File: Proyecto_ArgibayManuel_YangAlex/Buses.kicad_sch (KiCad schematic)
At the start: 6 parts, among them U6 MCP2551-I-P, X1 DB9, X2 DB9

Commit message: footprint
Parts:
- C5: renamed from C11; footprint (none) -> Capacitor_SMD:C_0805_2012Metric
- C6: renamed from C10; footprint (none) -> Capacitor_SMD:C_0805_2012Metric
- R10: renamed from R6; footprint (none) -> Resistor_THT:R_Axial_DIN0204_L3.6mm_D1.6mm_P1.90mm_Vertical
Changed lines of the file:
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@@
 		(dnp no)
 		(fields_autoplaced yes)
-		(property "Reference" "#PWR027"
+		(property "Reference" "#PWR020"
 			(at 55.88 53.34 0)
 			(effects
@@
 			(project "Proyecto_ArgibayManuel_YangAlex"
 				(path "/b2dde924-33f5-41ab-a1bf-811873450a89/310eabda-5b3c-4ba2-a48d-a60bed009d94"
-					(reference "#PWR027")
+					(reference "#PWR020")
 					(unit 1)
 				)
@@
 		(on_board yes)
 		(dnp no)
-		(property "Reference" "#PWR028"
+		(property "Reference" "#PWR019"
 			(at 35.56 74.93 0)
 			(effects
@@
 			(project "Proyecto_ArgibayManuel_YangAlex"
 				(path "/b2dde924-33f5-41ab-a1bf-811873450a89/310eabda-5b3c-4ba2-a48d-a60bed009d94"
-					(reference "#PWR028")
+					(reference "#PWR019")
 					(unit 1)
 				)
@@
 		(on_board yes)
 		(dnp no)
-		(property "Reference" "C10"
+		(property "Reference" "C6"
 			(at 145.288 58.166 90)
 			(effects
@@
 			)
 		)
-		(property "Footprint" ""
+		(property "Footprint" "Capacitor_SMD:C_0805_2012Metric"
 			(at 143.51 53.6448 0)
 			(effects
@@
 			(project "Proyecto_ArgibayManuel_YangAlex"
 				(path "/b2dde924-33f5-41ab-a1bf-811873450a89/310eabda-5b3c-4ba2-a48d-a60bed009d94"
-					(reference "C10")
+					(reference "C6")
 					(unit 1)
 				)
@@
 		(on_board yes)
 		(dnp no)
-		(property "Reference" "C11"
+		(property "Reference" "C5"
 			(at 144.78 38.608 90)
 			(effects
@@
 			)
 		)
-		(property "Footprint" ""
+		(property "Footprint" "Capacitor_SMD:C_0805_2012Metric"
 			(at 143.51 40.9448 0)
 			(effects
@@
 			(project "Proyecto_ArgibayManuel_YangAlex"
 				(path "/b2dde924-33f5-41ab-a1bf-811873450a89/310eabda-5b3c-4ba2-a48d-a60bed009d94"
-					(reference "C11")
+					(reference "C5")
 					(unit 1)
 				)
@@
 		(on_board yes)
 		(dnp no)
-		(property "Reference" "R6"
+		(property "Reference" "R10"
 			(at 137.16 46.9899 0)
 			(effects
@@
 			)
 		)
-		(property "Footprint" ""
+		(property "Footprint" "Resistor_THT:R_Axial_DIN0204_L3.6mm_D1.6mm_P1.90mm_Vertical"
 			(at 136.398 48.26 90)
 			(effects
@@
 			(project "Proyecto_ArgibayManuel_YangAlex"
 				(path "/b2dde924-33f5-41ab-a1bf-811873450a89/310eabda-5b3c-4ba2-a48d-a60bed009d94"
-					(reference "R6")
+					(reference "R10")
 					(unit 1)
 				)
@@
 		(on_board yes)
 		(dnp no)
-		(property "Reference" "#PWR07"
+		(property "Reference" "#PWR022"
 			(at 116.84 64.77 0)
 			(effects
@@
 			(project "Proyecto_ArgibayManuel_YangAlex"
 				(path "/b2dde924-33f5-41ab-a1bf-811873450a89/310eabda-5b3c-4ba2-a48d-a60bed009d94"
-					(reference "#PWR07")
+					(reference "#PWR022")
 					(unit 1)
 				)
@@
 		(on_board yes)
 		(dnp no)
-		(property "Reference" "#PWR022"
+		(property "Reference" "#PWR018"
 			(at 30.48 45.72 0)
 			(effects
@@
 			(project "Proyecto_ArgibayManuel_YangAlex"
 				(path "/b2dde924-33f5-41ab-a1bf-811873450a89/310eabda-5b3c-4ba2-a48d-a60bed009d94"
-					(reference "#PWR022")
-					(unit 1)
-				)
+					(reference "#PWR018")
+					(unit 1)
+				)

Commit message: sensor
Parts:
- removed X2: DB9, DB9:DB9, symbol DB9:DB9
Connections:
- net RC6 is gone; now on net GND: X1.3
- net CANH: now also X1.7
- net CANL: now also X1.2
- net GND: no longer X1.2
- net RC7: no longer names the net of X1.4
- net SCL: no longer names the net of X1.5
- net SDA: no longer names the net of X1.6
- no-connect marks 9 -> 5
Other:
- moved on the sheet: X1

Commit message: icsp
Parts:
- added J1: Conn_PIC_ICSP_ICD, symbol Connector:Conn_PIC_ICSP_ICD
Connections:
- net GND: now also J1.3 (VSS); no longer X1.3
- net VCC: now also J1.2 (VDD); no longer X1.1
- new net PGC: J1.5 (PGC/ICSPCLK)
- new net PGD: J1.4 (PGD/ICSPDAT)
- new net PGM: J1.6 (PGM/LVP)
- new net Vpp: J1.1 (~{MCLR}/VPP)
- no-connect marks 5 -> 7
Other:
- note added: "ICSP"

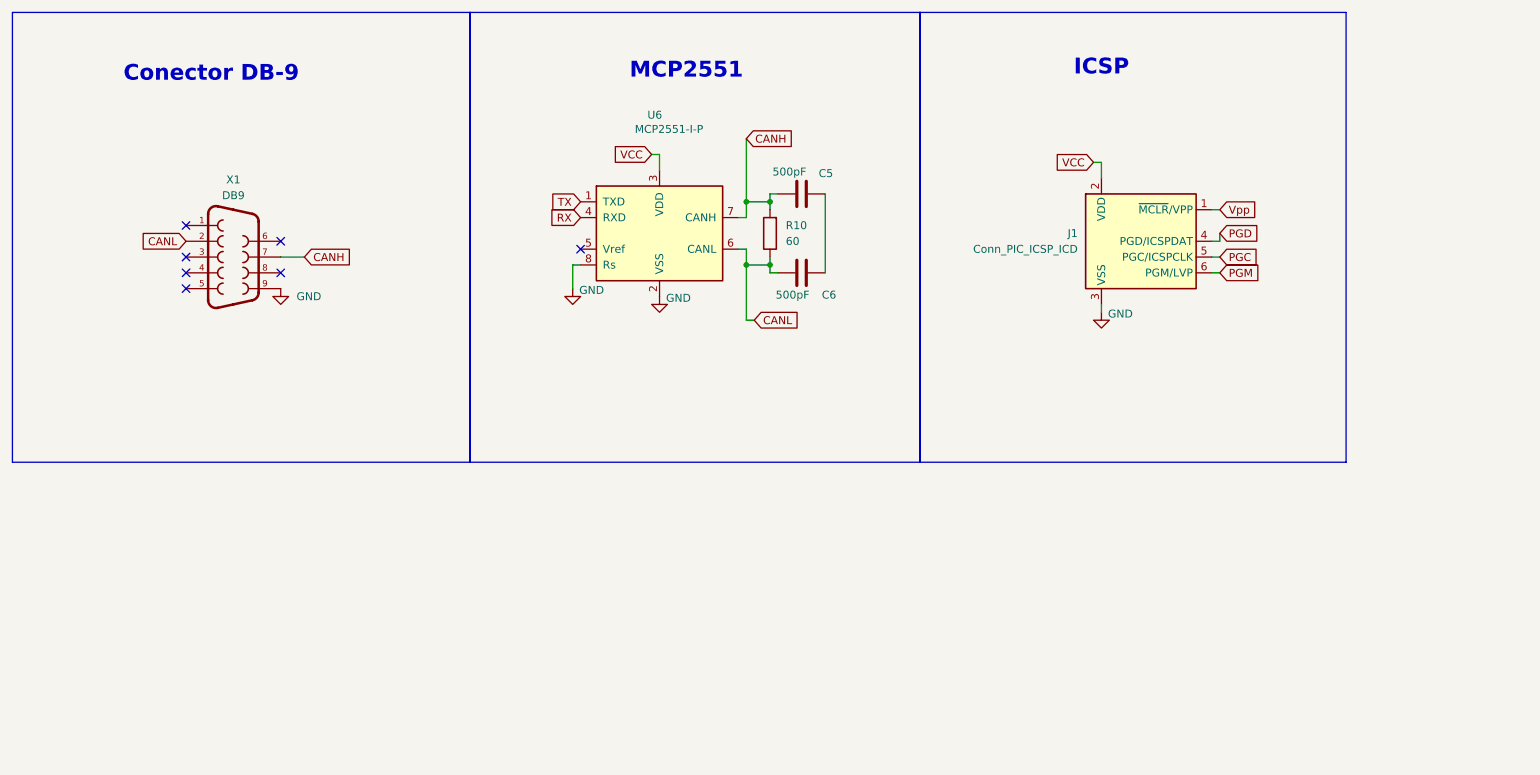
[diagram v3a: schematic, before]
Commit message: Arreglo net classes, agrego DB-9
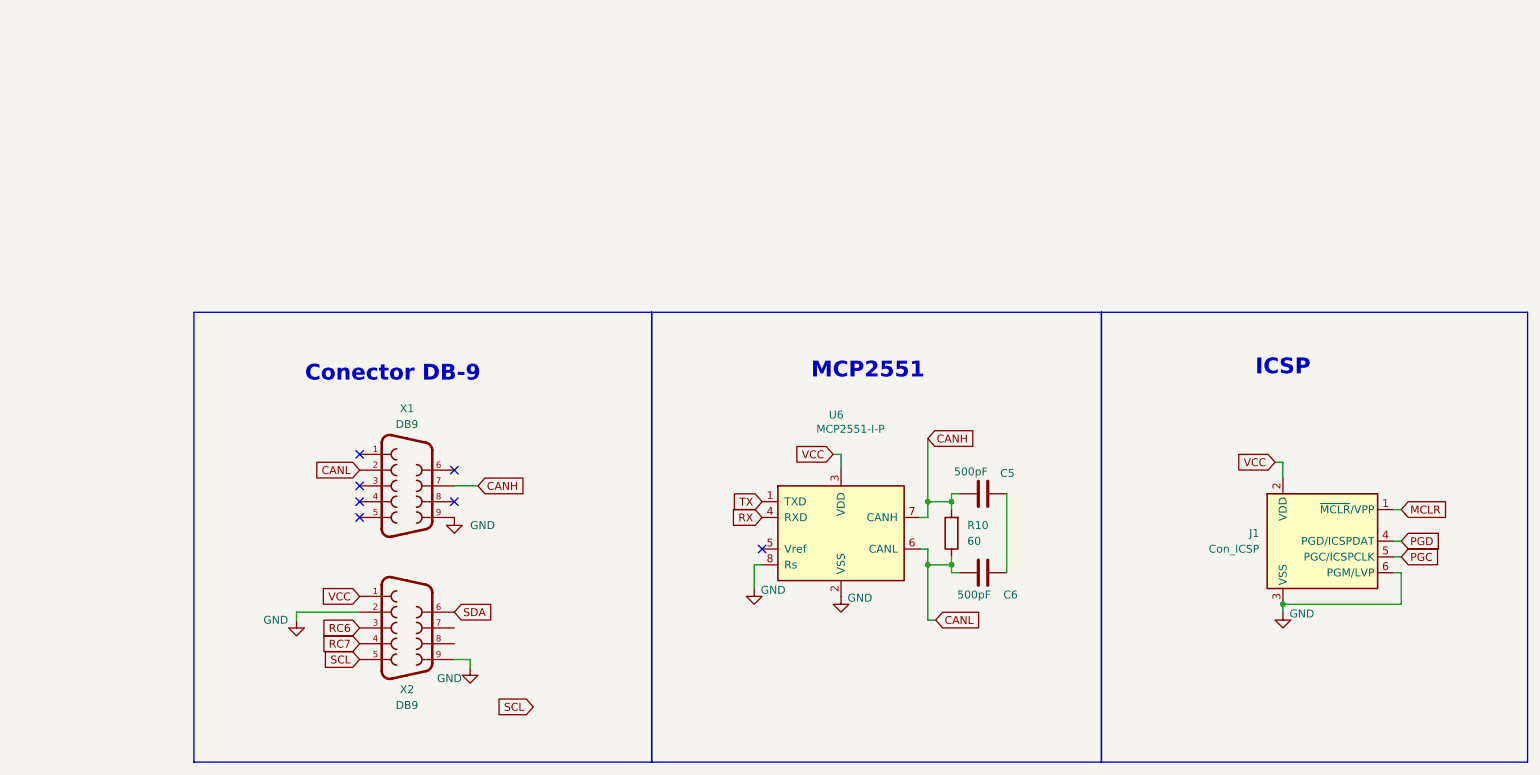
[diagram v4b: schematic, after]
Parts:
- added X2: DB9, DB9:DB9, symbol DB9:DB9
- J1: value Conn_PIC_ICSP_ICD -> Con_ICSP
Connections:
- net PGM is gone; now on net GND: J1.6 (PGM/LVP)
- net GND: now also X2.2, X2.9
- net VCC: now also X2.1
- net Vpp renamed MCLR
- new net RC6: X2.3
- new net RC7: X2.4
- new net SCL: X2.5
- new net SDA: X2.6
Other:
- company: (none) -> Universidad de Barcelona
- title: (none) -> Buses de comunicación
- moved on the sheet: C5, C6, J1, R10, U6, X1

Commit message: Empiezo layout, cambio footprints y arreglo esquematico
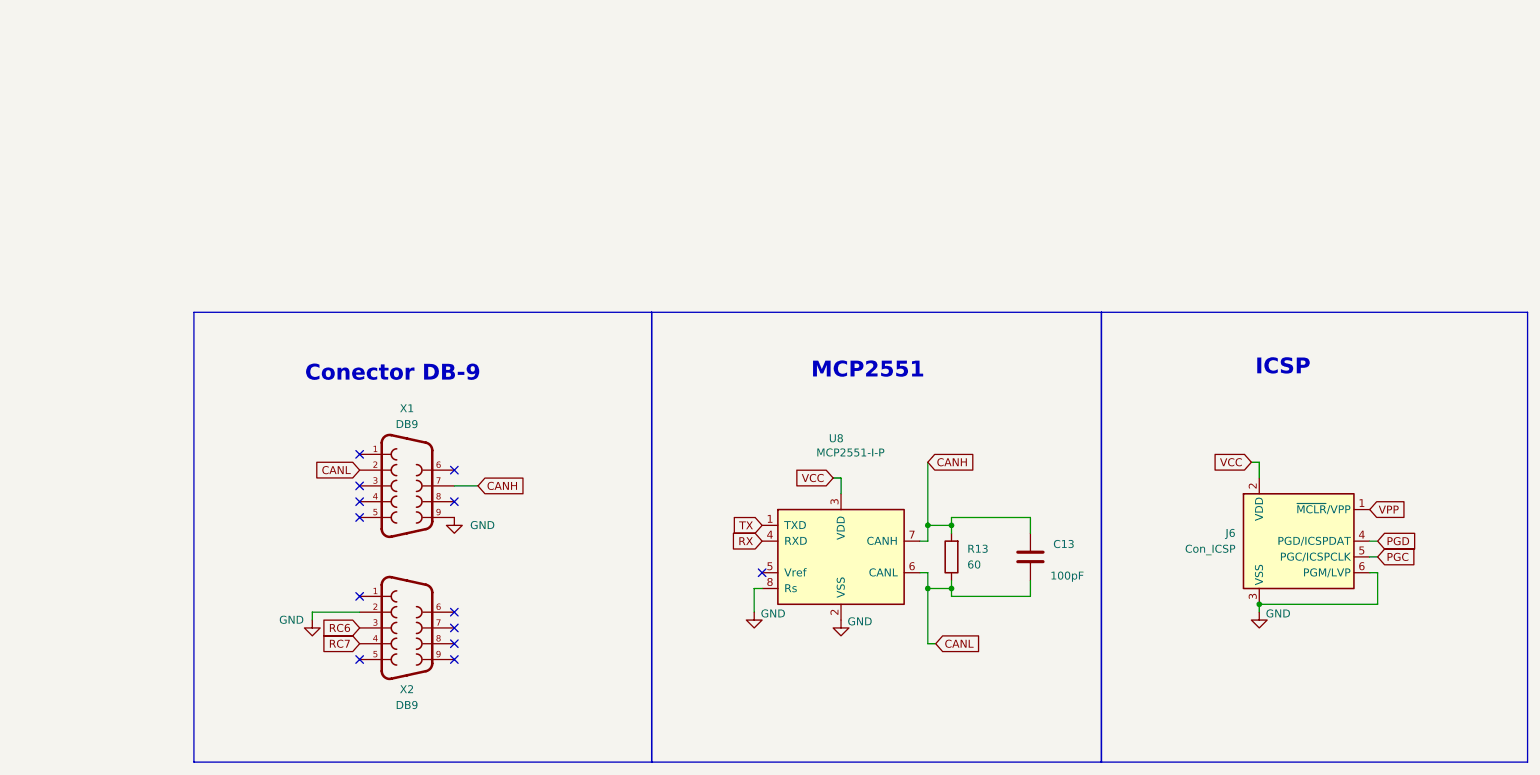
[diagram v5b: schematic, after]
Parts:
- removed C5, C6: 500pF, Capacitor_SMD:C_0805_2012Metric, symbol Device:C
- added C13: 100pF, Capacitor_SMD:C_0805_2012Metric, symbol Device:C
- J6: renamed from J1; footprint (none) -> Connector_PinHeader_2.54mm:PinHeader_1x06_P2.54mm_Vertical
- R13: renamed from R10; footprint Resistor_THT:R_Axial_DIN0204_L3.6mm_D1.6mm_P1.90mm_Vertical -> Resistor_SMD:R_0805_2012Metric
- X1, X2: footprint DB9:DB9 -> Footprints:DB9
- renumbered U6 to U8
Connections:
- net CANH: now also C13.2
- net CANL: now also C13.1
- net GND: no longer X2.9
- net VCC: no longer X2.1
- net MCLR renamed VPP
- net SCL: no longer names the net of X2.5
- net SDA: no longer names the net of X2.6
- no-connect marks 7 -> 13
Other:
- moved on the sheet: J6, R13, U8

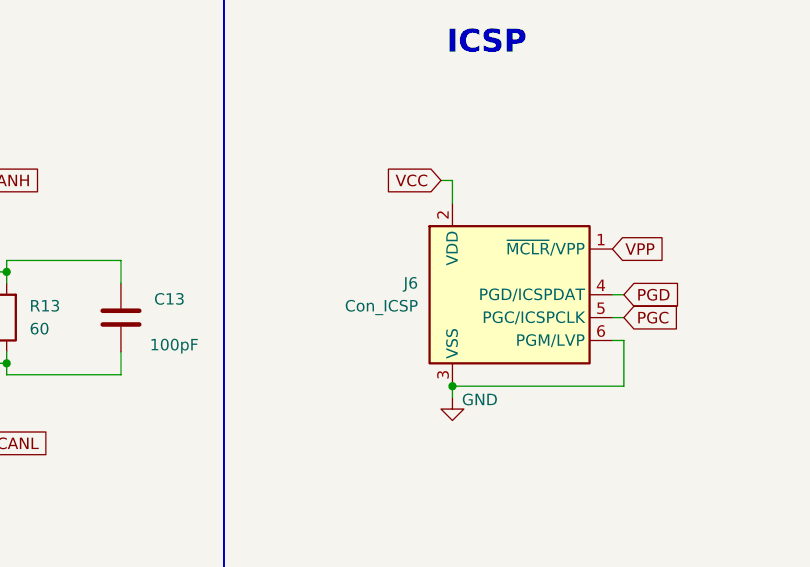
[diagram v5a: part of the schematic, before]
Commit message: Cambio de presentacion(esquematico,consumo,layout), minimas correciones en el esquematico
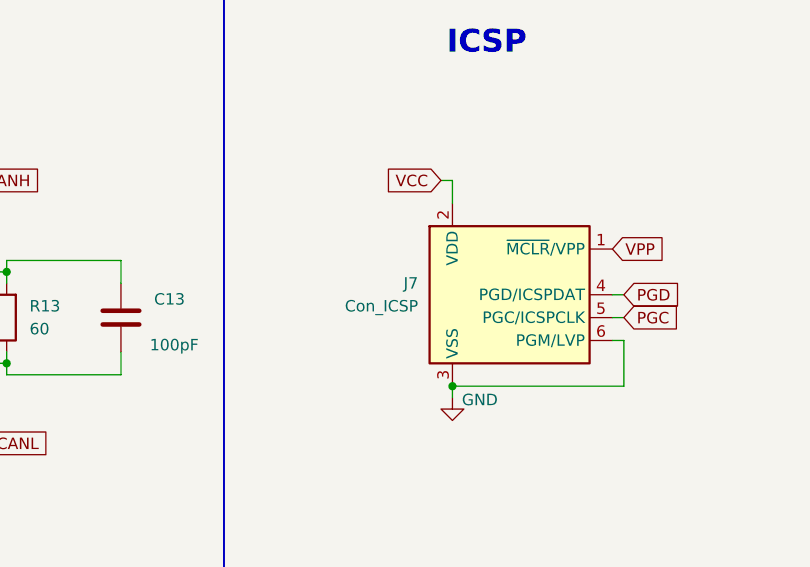
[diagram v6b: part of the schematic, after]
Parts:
- renumbered J6 to J7
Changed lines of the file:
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@@
 		(dnp no)
 		(fields_autoplaced yes)
-		(property "Reference" "#PWR034"
+		(property "Reference" "#PWR035"
 			(at 83.82 100.33 0)
 			(effects
@@
 			(project "Proyecto_ArgibayManuel_YangAlex"
 				(path "/b2dde924-33f5-41ab-a1bf-811873450a89/310eabda-5b3c-4ba2-a48d-a60bed009d94"
-					(reference "#PWR034")
+					(reference "#PWR035")
 					(unit 1)
 				)
@@
 		(dnp no)
 		(fields_autoplaced yes)
-		(property "Reference" "J6"
+		(property "Reference" "J7"
 			(at 209.55 96.5199 0)
 			(effects
@@
 			(project ""
 				(path "/b2dde924-33f5-41ab-a1bf-811873450a89/310eabda-5b3c-4ba2-a48d-a60bed009d94"
-					(reference "J6")
+					(reference "J7")
 					(unit 1)
 				)
@@
 		(on_board yes)
 		(dnp no)
-		(property "Reference" "#PWR037"
+		(property "Reference" "#PWR038"
 			(at 213.36 115.57 0)
 			(effects
@@
 			(project "Proyecto_ArgibayManuel_YangAlex"
 				(path "/b2dde924-33f5-41ab-a1bf-811873450a89/310eabda-5b3c-4ba2-a48d-a60bed009d94"
-					(reference "#PWR037")
+					(reference "#PWR038")
 					(unit 1)
 				)
@@
 		(on_board yes)
 		(dnp no)
-		(property "Reference" "#PWR035"
+		(property "Reference" "#PWR036"
 			(at 132.08 115.57 0)
 			(effects
@@
 			(project "Proyecto_ArgibayManuel_YangAlex"
 				(path "/b2dde924-33f5-41ab-a1bf-811873450a89/310eabda-5b3c-4ba2-a48d-a60bed009d94"
-					(reference "#PWR035")
+					(reference "#PWR036")
 					(unit 1)
 				)
@@
 		(on_board yes)
 		(dnp no)
-		(property "Reference" "#PWR036"
+		(property "Reference" "#PWR037"
 			(at 146.05 116.84 0)
 			(effects
@@
 			(project "Proyecto_ArgibayManuel_YangAlex"
 				(path "/b2dde924-33f5-41ab-a1bf-811873450a89/310eabda-5b3c-4ba2-a48d-a60bed009d94"
-					(reference "#PWR036")
+					(reference "#PWR037")
 					(unit 1)
 				)
@@
 		(on_board yes)
 		(dnp no)
-		(property "Reference" "#PWR033"
+		(property "Reference" "#PWR034"
 			(at 60.96 116.84 0)
 			(effects
@@
 			(project "Proyecto_ArgibayManuel_YangAlex"
 				(path "/b2dde924-33f5-41ab-a1bf-811873450a89/310eabda-5b3c-4ba2-a48d-a60bed009d94"
-					(reference "#PWR033")
-					(unit 1)
-				)
+					(reference "#PWR034")
+					(unit 1)
+				)

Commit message: Agrego cambios
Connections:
- net CANH renamed CAN+
- net CANL renamed CAN-
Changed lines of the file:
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@@
 		)
 	)
-	(global_label "CANH"
+	(global_label "CAN+"
 		(shape input)
 		(at 160.02 85.09 0)
@@
 		)
 		(property "Intersheetrefs" "${INTERSHEET_REFS}"
-			(at 168.0248 85.09 0)
+			(at 168.2667 85.09 0)
 			(effects
 				(font
@@
 		)
 	)
-	(global_label "CANL"
+	(global_label "CAN-"
 		(shape input)
 		(at 161.29 114.3 0)
@@
 		)
 		(property "Intersheetrefs" "${INTERSHEET_REFS}"
-			(at 168.9924 114.3 0)
+			(at 169.5367 114.3 0)
 			(effects
 				(font
@@
 		)
 	)
-	(global_label "CANL"
+	(global_label "CAN-"
 		(shape input)
 		(at 68.58 86.36 180)
@@
 		)
 		(property "Intersheetrefs" "${INTERSHEET_REFS}"
-			(at 60.8776 86.36 0)
+			(at 60.3333 86.36 0)
 			(effects
 				(font
@@
 		)
 	)
-	(global_label "CANH"
+	(global_label "CAN+"
 		(shape input)
 		(at 87.63 88.9 0)
@@
 		)
 		(property "Intersheetrefs" "${INTERSHEET_REFS}"
-			(at 95.6348 88.9 0)
+			(at 95.8767 88.9 0)
 			(effects
 				(font

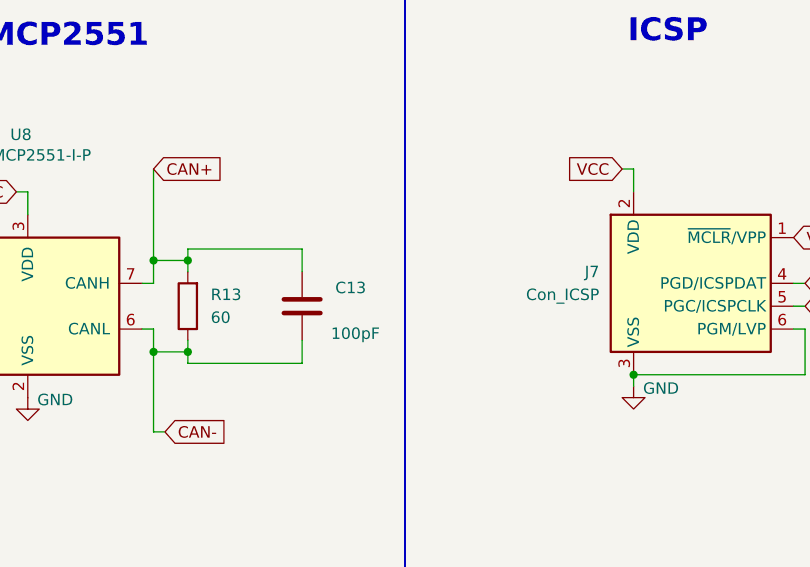
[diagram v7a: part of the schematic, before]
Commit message: Separacion de Botonera
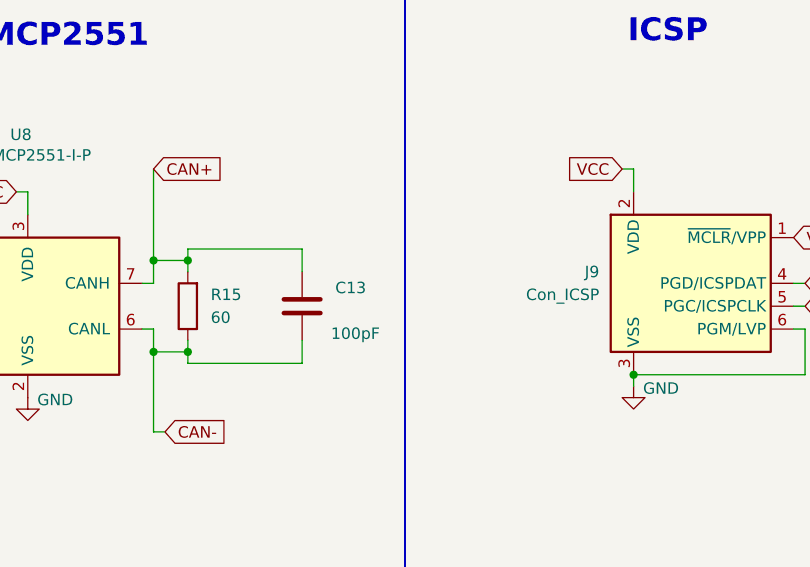
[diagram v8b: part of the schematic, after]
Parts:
- renumbered J7 to J9, R13 to R15
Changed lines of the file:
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@@
 		(dnp no)
 		(fields_autoplaced yes)
-		(property "Reference" "#PWR035"
+		(property "Reference" "#PWR038"
 			(at 83.82 100.33 0)
 			(effects
@@
 			(project "Proyecto_ArgibayManuel_YangAlex"
 				(path "/b2dde924-33f5-41ab-a1bf-811873450a89/310eabda-5b3c-4ba2-a48d-a60bed009d94"
-					(reference "#PWR035")
+					(reference "#PWR038")
 					(unit 1)
 				)
@@
 		(dnp no)
 		(fields_autoplaced yes)
-		(property "Reference" "J7"
+		(property "Reference" "J9"
 			(at 209.55 96.5199 0)
 			(effects
@@
 			(project ""
 				(path "/b2dde924-33f5-41ab-a1bf-811873450a89/310eabda-5b3c-4ba2-a48d-a60bed009d94"
-					(reference "J7")
+					(reference "J9")
 					(unit 1)
 				)
@@
 		(on_board yes)
 		(dnp no)
-		(property "Reference" "#PWR038"
+		(property "Reference" "#PWR041"
 			(at 213.36 115.57 0)
 			(effects
@@
 			(project "Proyecto_ArgibayManuel_YangAlex"
 				(path "/b2dde924-33f5-41ab-a1bf-811873450a89/310eabda-5b3c-4ba2-a48d-a60bed009d94"
-					(reference "#PWR038")
+					(reference "#PWR041")
 					(unit 1)
 				)
@@
 		(on_board yes)
 		(dnp no)
-		(property "Reference" "#PWR036"
+		(property "Reference" "#PWR039"
 			(at 132.08 115.57 0)
 			(effects
@@
 			(project "Proyecto_ArgibayManuel_YangAlex"
 				(path "/b2dde924-33f5-41ab-a1bf-811873450a89/310eabda-5b3c-4ba2-a48d-a60bed009d94"
-					(reference "#PWR036")
+					(reference "#PWR039")
 					(unit 1)
 				)
@@
 		(on_board yes)
 		(dnp no)
-		(property "Reference" "R13"
+		(property "Reference" "R15"
 			(at 166.37 99.0599 0)
 			(effects
@@
 			(project "Proyecto_ArgibayManuel_YangAlex"
 				(path "/b2dde924-33f5-41ab-a1bf-811873450a89/310eabda-5b3c-4ba2-a48d-a60bed009d94"
-					(reference "R13")
+					(reference "R15")
 					(unit 1)
 				)
@@
 		(on_board yes)
 		(dnp no)
-		(property "Reference" "#PWR037"
+		(property "Reference" "#PWR040"
 			(at 146.05 116.84 0)
 			(effects
@@
 			(project "Proyecto_ArgibayManuel_YangAlex"
 				(path "/b2dde924-33f5-41ab-a1bf-811873450a89/310eabda-5b3c-4ba2-a48d-a60bed009d94"
-					(reference "#PWR037")
+					(reference "#PWR040")
 					(unit 1)
 				)
@@
 		(on_board yes)
 		(dnp no)
-		(property "Reference" "#PWR034"
+		(property "Reference" "#PWR037"
 			(at 60.96 116.84 0)
 			(effects
@@
 			(project "Proyecto_ArgibayManuel_YangAlex"
 				(path "/b2dde924-33f5-41ab-a1bf-811873450a89/310eabda-5b3c-4ba2-a48d-a60bed009d94"
-					(reference "#PWR034")
-					(unit 1)
-				)
+					(reference "#PWR037")
+					(unit 1)
+				)
